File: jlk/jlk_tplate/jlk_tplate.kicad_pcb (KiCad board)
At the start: 2 copper layers, 252.8 x 108.8 mm, 38 parts, among them SW0 SWITCH_PUSH, SW1 SWITCH_PUSH, SW10 SWITCH_PUSH, SW11 SWITCH_PUSH, SW12 SWITCH_PUSH, SW13 SWITCH_PUSH, SW14 SWITCH_PUSH, SW15 SWITCH_PUSH, SW16 SWITCH_PUSH, SW17 SWITCH_PUSH, SW18 SWITCH_PUSH, SW19 SWITCH_PUSH, SW2 SWITCH_PUSH, SW20 SWITCH_PUSH, SW21 SWITCH_PUSH, SW22 SWITCH_PUSH, SW23 SWITCH_PUSH, SW24 SWITCH_PUSH, SW25 SWITCH_PUSH, SW26 SWITCH_PUSH, SW27 SWITCH_PUSH, SW28 SWITCH_PUSH, SW29 SWITCH_PUSH, SW3 SWITCH_PUSH, SW30 SWITCH_PUSH, SW31 SWITCH_PUSH, SW32 SWITCH_PUSH, SW33 SWITCH_PUSH, SW4 SWITCH_PUSH, SW5 SWITCH_PUSH, SW6 SWITCH_PUSH, SW7 SWITCH_PUSH, SW8 SWITCH_PUSH, SW9 SWITCH_PUSH

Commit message: Switched to SMD diode, col2row.
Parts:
- removed H12, H13, H14, H15: MountingHole, MountingHole:MountingHole_2.2mm_M2_ISO7380_Pad
- added H0: MountingHole, MountingHole:MountingHole_2.2mm_M2_ISO7380_Pad, F.Cu at (259.2, 97.0)
- added H1: MountingHole, MountingHole:MountingHole_2.2mm_M2_ISO7380_Pad, F.Cu at (190.2, 129.2)
- added H10: MountingHole, MountingHole:MountingHole_2.2mm_M2_ISO7380_Pad, F.Cu at (140.8, 69.4)
- added H11: MountingHole, MountingHole:MountingHole_2.2mm_M2_ISO7380_Pad, F.Cu at (133.9, 129.2)
- added H2: MountingHole, MountingHole:MountingHole_2.2mm_M2_ISO7380_Pad, F.Cu at (68.5, 45.5)
- added H3: MountingHole, MountingHole:MountingHole_2.2mm_M2_ISO7380_Pad, F.Cu at (183.3, 69.4)
- added H4: MountingHole, MountingHole:MountingHole_2.2mm_M2_ISO7380_Pad, F.Cu at (224.7, 113.1)
- added H5: MountingHole, MountingHole:MountingHole_2.2mm_M2_ISO7380_Pad, F.Cu at (64.9, 97.0)
- added H6: MountingHole, MountingHole:MountingHole_2.2mm_M2_ISO7380_Pad, F.Cu at (214.1, 45.2)
- added H7: MountingHole, MountingHole:MountingHole_2.2mm_M2_ISO7380_Pad, F.Cu at (110.0, 45.2)
- added H8: MountingHole, MountingHole:MountingHole_2.2mm_M2_ISO7380_Pad, F.Cu at (99.4, 113.1)
- added H9: MountingHole, MountingHole:MountingHole_2.2mm_M2_ISO7380_Pad, F.Cu at (256.1, 45.2)
- moved SW17 21.3 mm to (187.3, 78.0)
- moved SW0 21.3 mm to (64.0, 53.9)
- moved SW7 21.3 mm to (97.9, 71.2)
- moved SW27 21.3 mm to (234.2, 88.4)
- moved SW28 21.3 mm to (239.1, 53.9)
- moved SW16 21.3 mm to (129.9, 137.9)
- moved SW19 21.3 mm to (203.4, 112.6)
- moved SW2 21.3 mm to (47.9, 88.4)
- moved SW26 21.3 mm to (226.2, 71.1)
- moved SW9 21.3 mm to (119.5, 70.0)
- moved SW10 21.3 mm to (111.5, 87.2)
- moved SW20 21.3 mm to (194.2, 137.9)
- moved SW3 21.3 mm to (85.0, 53.9)
- moved SW5 21.3 mm to (68.9, 88.4)
- moved SW6 21.3 mm to (106.0, 53.9)
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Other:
- board size 252.8 x 108.8 mm -> 253.4 x 109.2 mm

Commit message: Changed the reset button on the jlk.
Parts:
- moved H5 22.6 mm to (47.7, 82.3)
- moved H6 21.0 mm to (196.9, 33.2)
- moved H9 21.0 mm to (238.9, 33.2)
- moved H1 18.4 mm to (179.8, 114.1)
- moved H3 18.4 mm to (172.9, 54.2)
- moved H4 17.6 mm to (209.2, 104.8)
- moved H10 17.5 mm to (132.1, 54.2)
- moved H11 17.5 mm to (125.3, 114.1)
- moved SW15 16.4 mm to (111.2, 99.2)
- moved SW22 16.4 mm to (203.1, 73.9)
- moved SW12 16.4 mm to (103.1, 116.5)
- moved SW8 16.4 mm to (80.4, 75.0)
- moved SW27 16.4 mm to (224.7, 75.0)
- moved SW25 16.4 mm to (208.6, 40.5)
- moved SW33 16.4 mm to (266.7, 75.0)
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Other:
- outline, holes or cut-outs redrawn

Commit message: Changed jlk for mounting promicro under the pcb.
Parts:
- removed H4, H6, H7, H8: MountingHole, MountingHole:MountingHole_2.2mm_M2_ISO7380_Pad
- moved H10 16.0 mm to (121.3, 65.9)
- moved H11 16.0 mm to (114.4, 125.7)
- moved H1 14.2 mm to (187.9, 125.7)
- moved H3 14.2 mm to (181.0, 65.9)
- moved H0 14.0 mm to (256.0, 96.2)
- moved SW4 14.0 mm to (66.0, 71.7)
- moved SW32 14.0 mm to (257.3, 71.7)
- moved SW22 14.0 mm to (201.7, 87.8)
- moved SW24 14.0 mm to (200.6, 130.3)
- moved SW10 14.0 mm to (100.6, 87.8)
- moved SW17 14.0 mm to (176.4, 78.5)
- moved SW14 14.0 mm to (117.8, 95.8)
- moved SW28 14.0 mm to (228.2, 54.4)
- moved SW3 14.0 mm to (74.1, 54.4)
- moved SW31 14.0 mm to (249.2, 54.4)
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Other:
- outline, holes or cut-outs redrawn

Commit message: Switched jlk to use nice!nano.
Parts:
- moved SW17 14.0 mm to (175.3, 64.6)
- moved SW19 14.0 mm to (191.4, 99.2)
- moved SW26 14.0 mm to (214.1, 57.7)
- moved H1 14.0 mm to (186.8, 111.8)
- moved H11 14.0 mm to (113.2, 111.8)
- moved H3 14.0 mm to (179.9, 52.0)
- moved H5 14.0 mm to (45.1, 82.3)
- moved SW1 14.0 mm to (43.9, 57.7)
- moved SW10 14.0 mm to (99.4, 73.8)
- moved SW14 14.0 mm to (116.7, 81.9)
- moved SW16 14.0 mm to (117.8, 124.5)
- moved SW33 14.0 mm to (264.2, 75.0)
- moved SW7 14.0 mm to (85.9, 57.8)
- moved SW8 14.0 mm to (77.9, 75.0)
- moved SW32 14.0 mm to (256.1, 57.7)
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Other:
- outline, holes or cut-outs redrawn

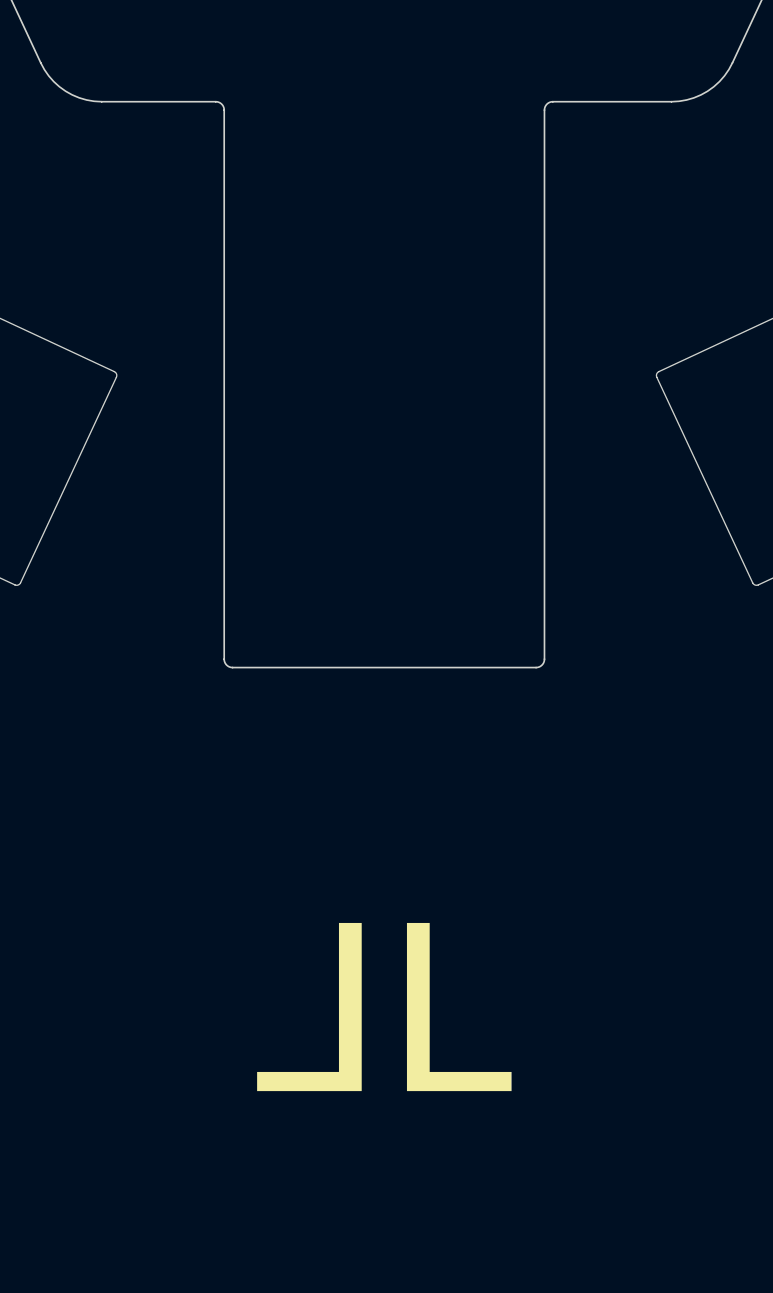
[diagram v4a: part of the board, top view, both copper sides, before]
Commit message: Moved mcu to underside of pcb, added battery jack.
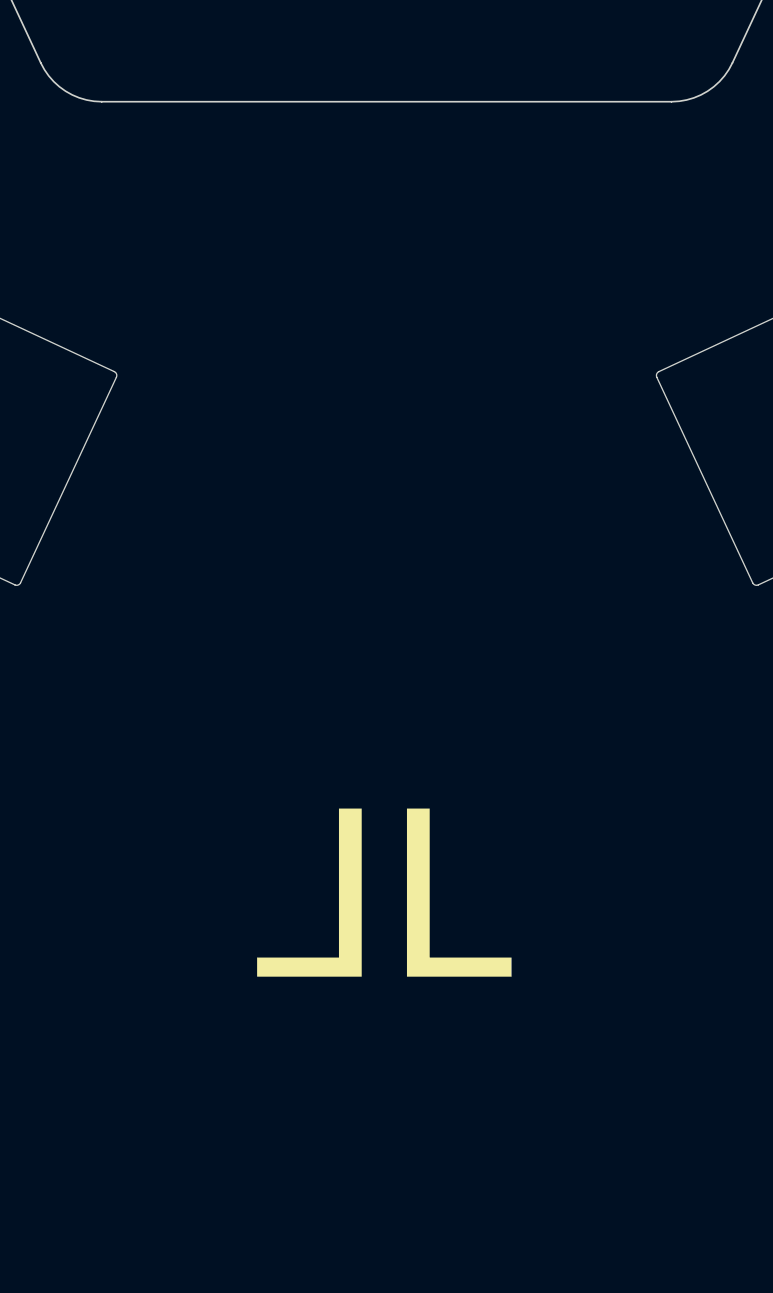
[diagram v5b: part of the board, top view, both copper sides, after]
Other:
- outline, holes or cut-outs redrawn
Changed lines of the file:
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@@
   (gr_line (start 180.088606 27.819841) (end 252.36344 27.819839)
     (stroke (width 0.1) (type default)) (layer "Edge.Cuts"))
-  (gr_line (start 133.050088 45.085) (end 139.835 45.085)
-    (stroke (width 0.1) (type default)) (layer "Edge.Cuts"))
-  (gr_arc (start 159.385 78.24) (mid 159.238553 78.593553) (end 158.885 78.74)
+  (gr_line (start 133.050088 45.085) (end 166.941167 45.085011)
     (stroke (width 0.1) (type default)) (layer "Edge.Cuts"))
   (gr_arc (start 133.050088 45.085) (mid 130.900861 44.458594) (end 129.424852 42.775477)
-    (stroke (width 0.1) (type default)) (layer "Edge.Cuts"))
-  (gr_arc (start 139.835 45.085) (mid 140.188553 45.231447) (end 140.335 45.585)
     (stroke (width 0.1) (type default)) (layer "Edge.Cuts"))
   (gr_line (start 129.424852 42.775477) (end 123.52788 30.129359)
@@
   (gr_arc (start 166.941162 119.86971) (mid 169.090333 120.496185) (end 170.566395 122.179241)
     (stroke (width 0.1) (type default)) (layer "Edge.Cuts"))
-  (gr_line (start 140.835 78.74) (end 158.885 78.74)
-    (stroke (width 0.1) (type default)) (layer "Edge.Cuts"))
   (gr_arc (start 122.662246 136.681726) (mid 122.380103 136.940239) (end 121.997784 136.923574)
     (stroke (width 0.1) (type default)) (layer "Edge.Cuts"))
@@
     (stroke (width 0.1) (type default)) (layer "Edge.Cuts"))
   (gr_line (start 47.627803 27.819845) (end 119.902646 27.81983)
-    (stroke (width 0.1) (type default)) (layer "Edge.Cuts"))
-  (gr_line (start 159.385 78.24) (end 159.385 45.585001)
     (stroke (width 0.1) (type default)) (layer "Edge.Cuts"))
   (gr_arc (start 170.566399 42.775483) (mid 169.090383 44.458595) (end 166.941167 45.085011)
@@
   (gr_line (start 133.05009 119.869718) (end 166.941162 119.86971)
     (stroke (width 0.1) (type default)) (layer "Edge.Cuts"))
-  (gr_arc (start 140.835 78.74) (mid 140.481447 78.593553) (end 140.335 78.24)
-    (stroke (width 0.1) (type default)) (layer "Edge.Cuts"))
-  (gr_line (start 140.335 45.585) (end 140.335 78.24)
-    (stroke (width 0.1) (type default)) (layer "Edge.Cuts"))
   (gr_arc (start 23.525394 79.851168) (mid 23.314731 79.569404) (end 23.341625 79.218631)
     (stroke (width 0.1) (type default)) (layer "Edge.Cuts"))
   (gr_arc (start 47.174647 28.108539) (mid 47.359136 27.898125) (end 47.627803 27.819845)
-    (stroke (width 0.1) (type default)) (layer "Edge.Cuts"))
-  (gr_arc (start 159.385 45.585001) (mid 159.531447 45.231447) (end 159.885001 45.085001)
-    (stroke (width 0.1) (type default)) (layer "Edge.Cuts"))
-  (gr_line (start 159.885001 45.085001) (end 166.941167 45.085011)
     (stroke (width 0.1) (type default)) (layer "Edge.Cuts"))
   (gr_arc (start 119.902646 27.81983) (mid 122.051836 28.446291) (end 123.52788 30.129359)
@@
   (gr_line (start 212.040554 121.047164) (end 177.993476 136.923578)
     (stroke (width 0.1) (type default)) (layer "Edge.Cuts"))
-  (gr_text "L" (at 149.86 99.304859) (layer "B.SilkS")
+  (gr_text "L" (at 149.86 92.5) (layer "B.SilkS")
     (effects (font (face "Arial") (size 10 10) (thickness 0.15)) (justify left))
     (render_cache "L" 0
       (polygon
         (pts
-          (xy 150.890704 103.454859)          (xy 150.890704 93.294356)          (xy 152.22427 93.294356)          (xy 152.22427 102.204335)
-          (xy 157.1824 102.204335)          (xy 157.1824 103.454859)
+          (xy 150.890704 96.65)          (xy 150.890704 86.489497)          (xy 152.22427 86.489497)          (xy 152.22427 95.399476)
+          (xy 157.1824 95.399476)          (xy 157.1824 96.65)
         )
       )
@@
     )
   )
-  (gr_text "L" (at 149.86 99.304859) (layer "B.SilkS")
+  (gr_text "L" (at 149.86 92.5) (layer "B.SilkS")
     (effects (font (face "Arial") (size 10 10) (thickness 0.15)) (justify left mirror))
     (render_cache "L" 0
       (polygon
         (pts
-          (xy 148.829295 103.454859)          (xy 148.829295 93.294356)          (xy 147.495729 93.294356)          (xy 147.495729 102.204335)
-          (xy 142.537599 102.204335)          (xy 142.537599 103.454859)
+          (xy 148.829295 96.65)          (xy 148.829295 86.489497)          (xy 147.495729 86.489497)          (xy 147.495729 95.399476)
+          (xy 142.537599 95.399476)          (xy 142.537599 96.65)
         )
       )
     )
   )
-  (gr_text "L" (at 149.86 99.304859) (layer "F.SilkS")
+  (gr_text "L" (at 149.86 92.5) (layer "F.SilkS")
     (effects (font (face "Arial") (size 10 10) (thickness 0.15)) (justify left mirror))
     (render_cache "L" 0
       (polygon
         (pts
-          (xy 148.829295 103.454859)          (xy 148.829295 93.294356)          (xy 147.495729 93.294356)          (xy 147.495729 102.204335)
-          (xy 142.537599 102.204335)          (xy 142.537599 103.454859)
+          (xy 148.829295 96.65)          (xy 148.829295 86.489497)          (xy 147.495729 86.489497)          (xy 147.495729 95.399476)
+          (xy 142.537599 95.399476)          (xy 142.537599 96.65)
         )
       )
     )
   )
-  (gr_text "L" (at 149.86 99.304859) (layer "F.SilkS")
+  (gr_text "L" (at 149.86 92.5) (layer "F.SilkS")
     (effects (font (face "Arial") (size 10 10) (thickness 0.15)) (justify left))
     (render_cache "L" 0
       (polygon
         (pts
-          (xy 150.890704 103.454859)          (xy 150.890704 93.294356)          (xy 152.22427 93.294356)          (xy 152.22427 102.204335)
-          (xy 157.1824 102.204335)          (xy 157.1824 103.454859)
+          (xy 150.890704 96.65)          (xy 150.890704 86.489497)          (xy 152.22427 86.489497)          (xy 152.22427 95.399476)
+          (xy 157.1824 95.399476)          (xy 157.1824 96.65)
         )
       )

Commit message: Small changes.
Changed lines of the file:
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@@
     (pad "1" thru_hole circle (at 0 0 335) (size 3.5 3.5) (drill 2.2) (layers "*.Cu" "*.Mask"))
   )
+  (gr_circle (center 149.86 92.5) (end 159.86 92.5)
+    (stroke (width 1) (type default)) (fill none) (layer "B.SilkS"))
+  (gr_circle (center 149.86 92.5) (end 159.86 92.5)
+    (stroke (width 1) (type default)) (fill none) (layer "F.SilkS"))
   (gr_line (start 129.424851 122.179246) (end 122.662246 136.681726)
     (stroke (width 0.1) (type default)) (layer "Edge.Cuts"))

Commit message: Added filled polygons on top and bottom plates.
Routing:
- added copper zone on B.Cu, net (none)
- added copper zone on F.Cu, net (none)
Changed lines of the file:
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@@
+    )
+  )
+  (zone (net 0) (net_name "") (layers "F&B.Cu") (hatch edge 0.5)
+    (connect_pads (clearance 0.508))
+    (min_thickness 0.25) (filled_areas_thickness no)
+    (fill yes (thermal_gap 0.5) (thermal_bridge_width 0.5) (island_removal_mode 1) (island_area_min 10))
+    (polygon
+      (pts
+        (xy 22 26.5)
+        (xy 277.5 26.5)
+        (xy 277.5 138.5)
+        (xy 277 139)
+        (xy 22.5 139)
+        (xy 22 138.5)
+      )
     )
   )
